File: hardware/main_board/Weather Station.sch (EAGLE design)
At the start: 24 parts, among them J2 RJ12, U1 328P, U2 MCP1703T-3302E/CB, U3 W25X40CLSNIG, X2 B2B-PH-K-S, X3 B2B-XH-2, Y1 8MHz

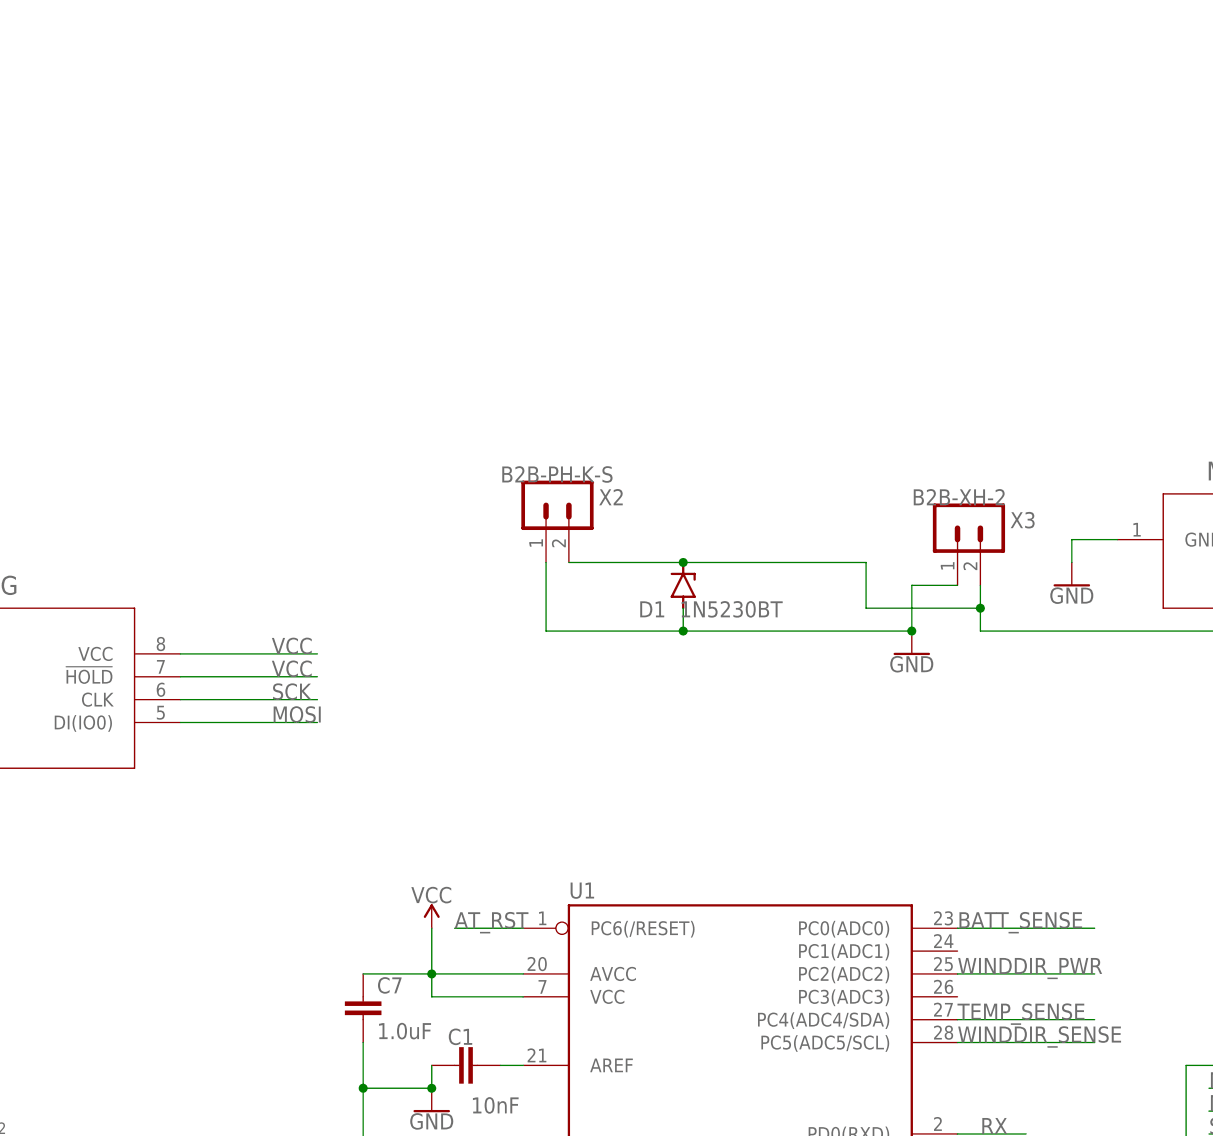
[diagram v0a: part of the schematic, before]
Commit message: Fixed sleep logic Decreased radio transition times Changed default spreading factor Fixed internal temperature calibration Fixed lack of length prepending weather messages Changed diode for TL431 (TODO: Test unregulated charging, change to PWM if necessary)
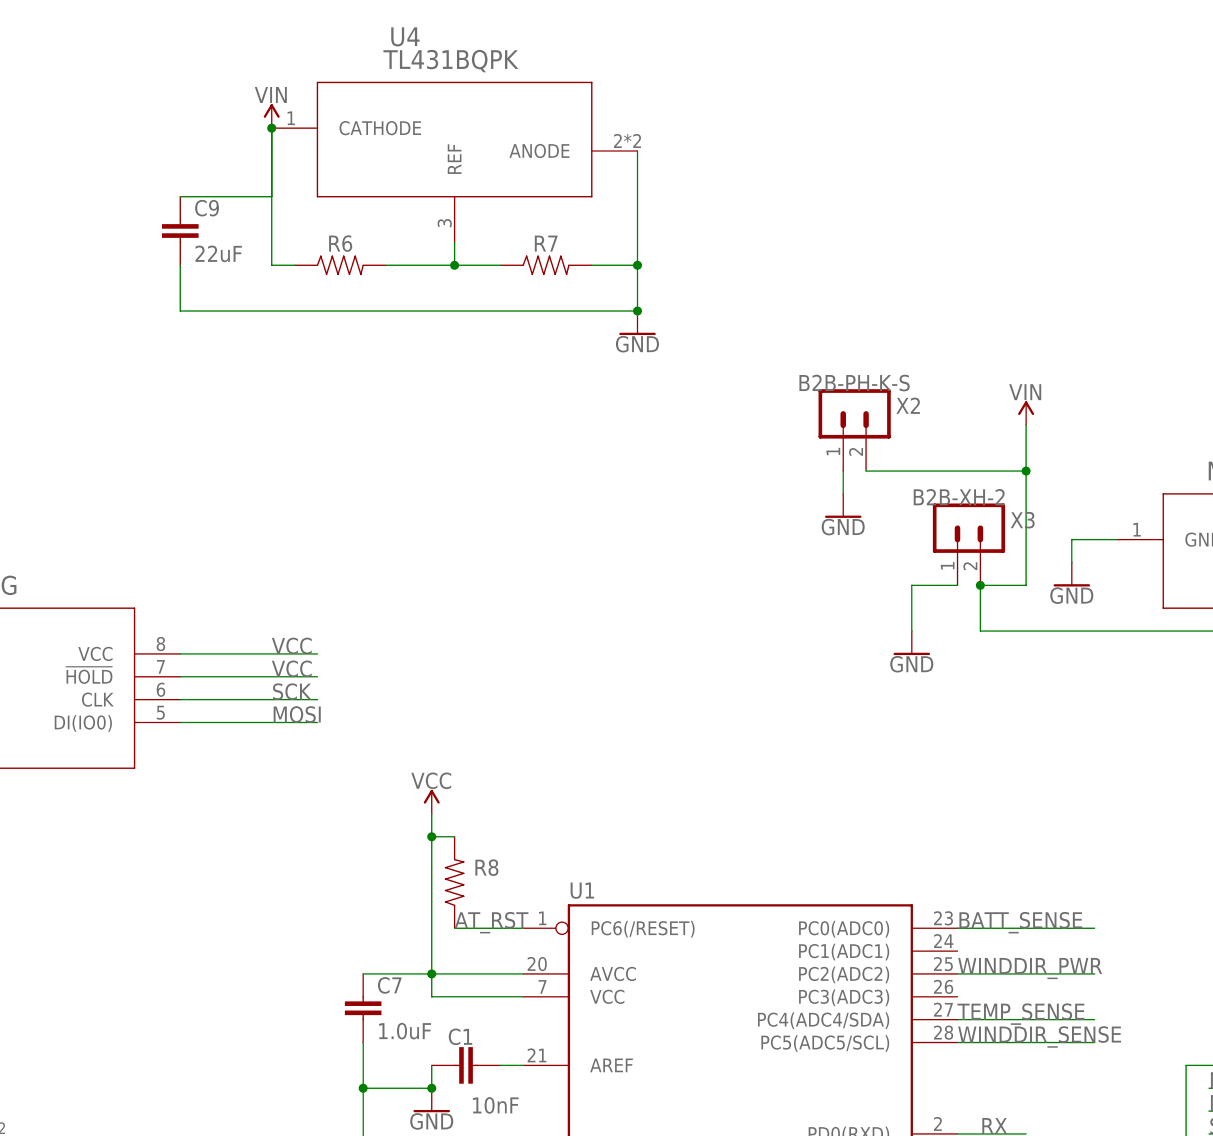
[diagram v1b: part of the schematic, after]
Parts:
- removed D1: 1N5230BT, diode:1N4728
- added C9: 22uF, SparkFun-Capacitors:22UF-0805-6.3V-20%
- added R6, R7, R8: (no value), SparkFun-Resistors:RESISTOR0805
- added U4: TL431BQPK, my-components:TL431BQPK
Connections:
- removed net N$9: C3.1, D1.C, R3.1, U2.VIN, X2.2, X3.2
- new net N$1: R6.2, R7.1, U4.REF
- new net VIN: C3.1, C9.1, R3.1, R6.1, U2.VIN, U4.CATHODE, X2.2, X3.2
- net AT_RST: now also R8.1
- net GND: now also C9.2, R7.2, U4.ANODE; no longer D1.A
- net VCC: now also R8.2
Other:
- moved on the sheet: X2

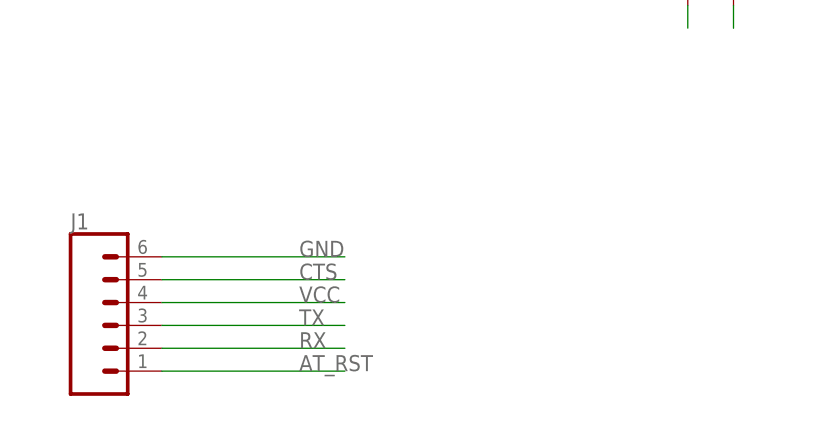
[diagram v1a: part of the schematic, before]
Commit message: Added wind calibration. Started using namespaces. Added indicator LEDs
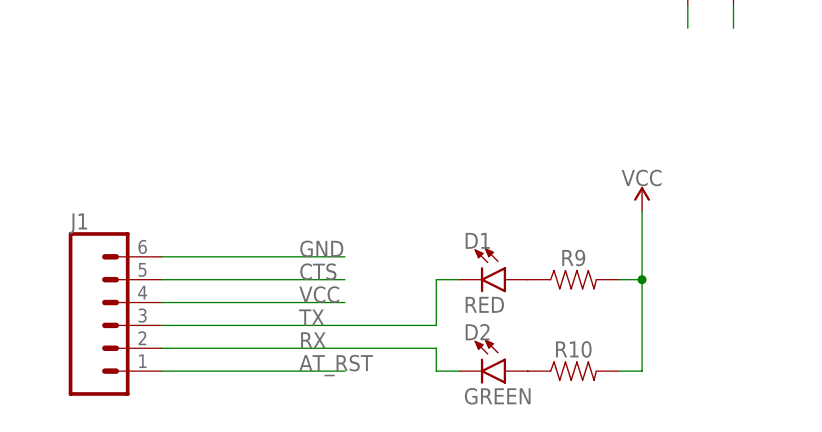
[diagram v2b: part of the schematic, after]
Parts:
- added D1: RED, SparkFun-LED:LED-RED1206
- added D2: GREEN, SparkFun-LED:LED-GREEN1206
- added R10, R9: (no value), SparkFun-Resistors:RESISTOR0805
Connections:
- new net N$4: D1.A, R9.1
- new net N$6: D2.A, R10.1
- net RX: now also D2.C
- net TX: now also D1.C
- net VCC: now also R10.2, R9.2
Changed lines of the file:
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@@
 <part name="C9" library="SparkFun-Capacitors" library_urn="urn:adsk.eagle:library:510" deviceset="22UF" device="-0805-6.3V-20%" package3d_urn="urn:adsk.eagle:package:37429/1" value="22uF"/>
 <part name="R8" library="SparkFun-Resistors" library_urn="urn:adsk.eagle:library:532" deviceset="RESISTOR" device="0805" package3d_urn="urn:adsk.eagle:package:39651/1" value=" "/>
+<part name="D1" library="SparkFun-LED" library_urn="urn:adsk.eagle:library:529" deviceset="LED-RED" device="1206" package3d_urn="urn:adsk.eagle:package:39352/1" value="RED"/>
+<part name="D2" library="SparkFun-LED" library_urn="urn:adsk.eagle:library:529" deviceset="LED-GREEN" device="1206" package3d_urn="urn:adsk.eagle:package:39352/1" value="GREEN"/>
+<part name="SUPPLY6" library="SparkFun-PowerSymbols" library_urn="urn:adsk.eagle:library:530" deviceset="VCC" device=""/>
+<part name="R9" library="SparkFun-Resistors" library_urn="urn:adsk.eagle:library:532" deviceset="RESISTOR" device="0805" package3d_urn="urn:adsk.eagle:package:39651/1" value=" "/>
+<part name="R10" library="SparkFun-Resistors" library_urn="urn:adsk.eagle:library:532" deviceset="RESISTOR" device="0805" package3d_urn="urn:adsk.eagle:package:39651/1" value=" "/>
 </parts>
 <sheets>
@@
 <attribute name="NAME" x="8.636" y="73.66" size="1.778" layer="95" font="vector" rot="R180" align="bottom-center"/>
 <attribute name="VALUE" x="6.604" y="71.12" size="1.778" layer="96" font="vector" rot="R90" align="top-center"/>
+</instance>
+<instance part="D1" gate="G$1" x="132.08" y="-17.78" smashed="yes" rot="R270">
+<attribute name="NAME" x="127.508" y="-14.351" size="1.778" layer="95" font="vector"/>
+<attribute name="VALUE" x="127.508" y="-19.685" size="1.778" layer="96" font="vector" align="top-left"/>
+</instance>
+<instance part="D2" gate="G$1" x="132.08" y="-27.94" smashed="yes" rot="R270">
+<attribute name="NAME" x="127.508" y="-24.511" size="1.778" layer="95" font="vector"/>
+<attribute name="VALUE" x="127.508" y="-29.845" size="1.778" layer="96" font="vector" align="top-left"/>
+</instance>
+<instance part="SUPPLY6" gate="G$1" x="147.32" y="-10.16" smashed="yes">
+<attribute name="VALUE" x="147.32" y="-7.366" size="1.778" layer="96" align="bottom-center"/>
+</instance>
+<instance part="R9" gate="G$1" x="139.7" y="-17.78" smashed="yes">
+<attribute name="NAME" x="139.7" y="-16.256" size="1.778" layer="95" font="vector" align="bottom-center"/>
+<attribute name="VALUE" x="139.7" y="-19.304" size="1.778" layer="96" font="vector" align="top-center"/>
+</instance>
+<instance part="R10" gate="G$1" x="139.7" y="-27.94" smashed="yes">
+<attribute name="NAME" x="139.7" y="-26.416" size="1.778" layer="95" font="vector" align="bottom-center"/>
+<attribute name="VALUE" x="139.7" y="-29.464" size="1.778" layer="96" font="vector" align="top-center"/>
 </instance>
 </instances>
@@
 <label x="-15.24" y="93.98" size="1.778" layer="95"/>
 </segment>
+<segment>
+<pinref part="R10" gate="G$1" pin="2"/>
+<pinref part="SUPPLY6" gate="G$1" pin="VCC"/>
+<wire x1="144.78" y1="-27.94" x2="147.32" y2="-27.94" width="0.1524" layer="91"/>
+<wire x1="147.32" y1="-27.94" x2="147.32" y2="-17.78" width="0.1524" layer="91"/>
+<pinref part="R9" gate="G$1" pin="2"/>
+<wire x1="147.32" y1="-17.78" x2="147.32" y2="-10.16" width="0.1524" layer="91"/>
+<wire x1="144.78" y1="-17.78" x2="147.32" y2="-17.78" width="0.1524" layer="91"/>
+<junction x="147.32" y="-17.78"/>
+</segment>
 </net>
 <net name="MISO" class="0">
@@
 <segment>
 <pinref part="J1" gate="G$1" pin="2"/>
-<wire x1="93.98" y1="-25.4" x2="114.3" y2="-25.4" width="0.1524" layer="91"/>
+<wire x1="93.98" y1="-25.4" x2="124.46" y2="-25.4" width="0.1524" layer="91"/>
 <label x="109.22" y="-25.4" size="1.778" layer="95"/>
+<pinref part="D2" gate="G$1" pin="C"/>
+<wire x1="124.46" y1="-25.4" x2="124.46" y2="-27.94" width="0.1524" layer="91"/>
+<wire x1="124.46" y1="-27.94" x2="127" y2="-27.94" width="0.1524" layer="91"/>
 </segment>
 </net>
@@
 <segment>
 <pinref part="J1" gate="G$1" pin="3"/>
-<wire x1="93.98" y1="-22.86" x2="114.3" y2="-22.86" width="0.1524" layer="91"/>
+<wire x1="93.98" y1="-22.86" x2="124.46" y2="-22.86" width="0.1524" layer="91"/>
 <label x="109.22" y="-22.86" size="1.778" layer="95"/>
+<pinref part="D1" gate="G$1" pin="C"/>
+<wire x1="124.46" y1="-22.86" x2="124.46" y2="-17.78" width="0.1524" layer="91"/>
+<wire x1="124.46" y1="-17.78" x2="127" y2="-17.78" width="0.1524" layer="91"/>
 </segment>
 </net>
@@
 <segment>
 <pinref part="U1" gate="G$1" pin="PC2(ADC2)"/>
+<label x="60.96" y="60.96" size="1.778" layer="95"/>
 <wire x1="60.96" y1="60.96" x2="76.2" y2="60.96" width="0.1524" layer="91"/>
-<label x="60.96" y="60.96" size="1.778" layer="95"/>
 </segment>
 <segment>
@@
 </segment>
 </net>
+<net name="N$4" class="0">
+<segment>
+<pinref part="D1" gate="G$1" pin="A"/>
+<pinref part="R9" gate="G$1" pin="1"/>
+</segment>
+</net>
+<net name="N$6" class="0">
+<segment>
+<pinref part="D2" gate="G$1" pin="A"/>
+<pinref part="R10" gate="G$1" pin="1"/>
+</segment>
+</net>

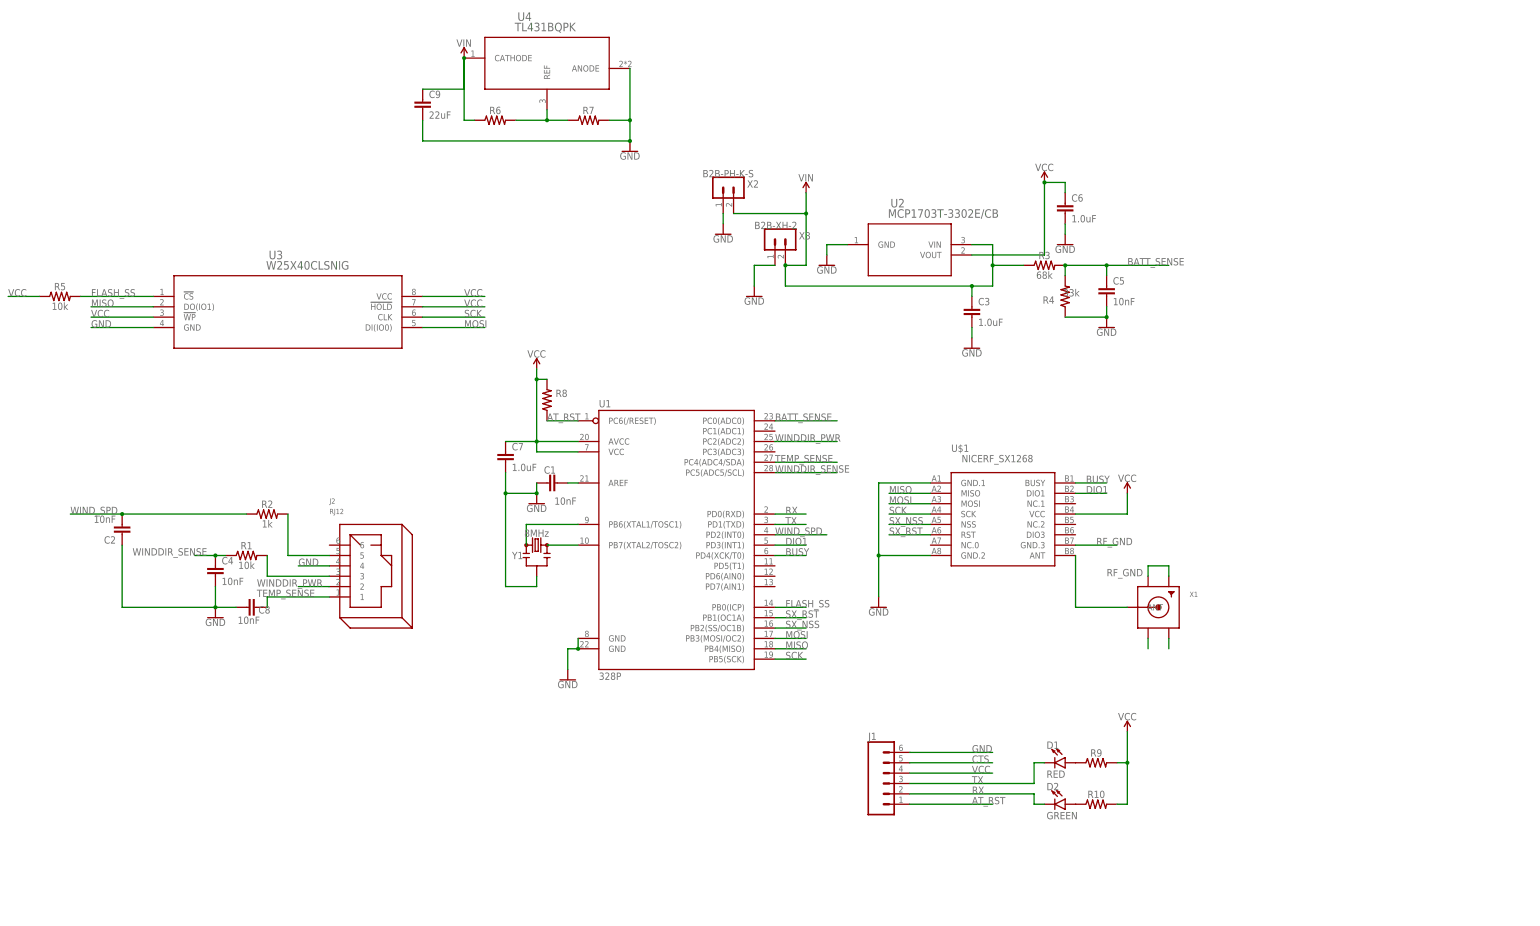
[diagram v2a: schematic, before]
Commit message: Added PWM charge control circuitry
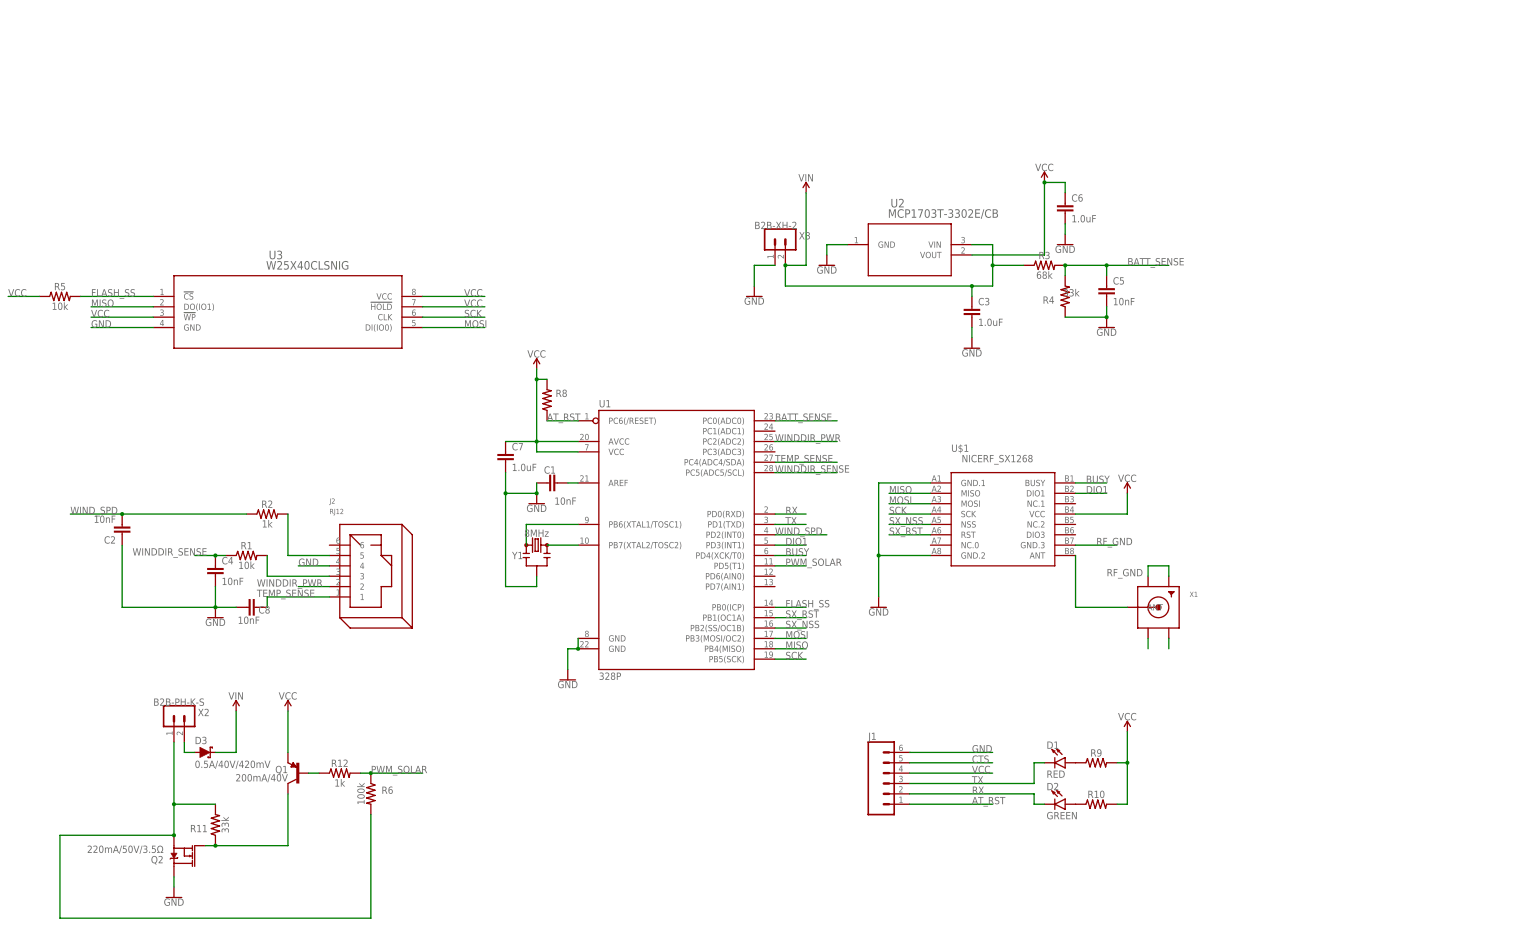
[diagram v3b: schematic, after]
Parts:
- removed C9: 22uF, SparkFun-Capacitors:22UF-0805-6.3V-20%
- removed R7: (no value), SparkFun-Resistors:RESISTOR0805
- removed U4: TL431BQPK, my-components:TL431BQPK
- added D3: 0.5A/40V/420mV, SparkFun-DiscreteSemi:DIODE-SCHOTTKY-PMEG4005EJ
- added Q1: 200mA/40V, SparkFun-DiscreteSemi:TRANS_PNP-PMBT3906|MMBT3906L
- added Q2: 220mA/50V/3.5Ω, SparkFun-DiscreteSemi:MOSFET-NCH-BSS138
- added R11: 33k, SparkFun-Resistors:RESISTOR0805
- added R12: 1k, SparkFun-Resistors:RESISTOR0805
- R6: value (none) -> 100k
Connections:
- removed net N$1: R6.2, R7.1, U4.REF
- new net N$12: Q1.C, Q2.G, R11.1
- new net N$13: Q1.B, R12.1
- new net N$14: D3.A, X2.2
- new net N$9: Q2.S, R11.2, R6.2, X2.1
- new net PWM_SOLAR: R12.2, R6.1, U1.PD5(T1)
- net GND: now also Q2.D; no longer C9.2, R7.2, U4.ANODE, X2.1
- net VCC: now also Q1.E
- net VIN: now also D3.C; no longer C9.1, R6.1, U4.CATHODE, X2.2
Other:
- moved on the sheet: R6, X2
